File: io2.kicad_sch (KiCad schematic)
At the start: 67 parts, among them IC1 ILD217T, IC2 ILD217T, Q10 BC846, Q11 BC846, Q8 BC846, Q9 BC846, U11 74HC14, U12 74HC165, X3 Conn_DI

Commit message: Ref 2.4
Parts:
- removed PS2: 1S4E_0505S1U, custom_th:Converter_DCDC_GAPTEC_1S4E_S1U, symbol Converter_DCDC:MEE1S0303SC
- added PS2: (no value), symbol lcsc:B0505S-1WR2_C909796
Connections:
- net +5V: now also C13.2, PS2.2 (Vin); no longer C13.1
- net 5V_1: now also PS2.4 (Vo)
- net GND: now also C13.1, PS2.1 (GND); no longer C13.2
- net GND1: now also PS2.3 (0V)
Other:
- moved on the sheet: C13
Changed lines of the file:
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@@
   (title_block
     (title "BSC")
-    (date "2023-03-30")
-    (rev "2.3")
+    (date "2023-06-25")
+    (rev "2.4")
   )
   (junction (at 115.57 118.745) (diameter 0) (color 0 0 0 0)
   )
-  (junction (at 171.45 154.305) (diameter 0) (color 0 0 0 0)
-  )
-  (junction (at 171.45 149.225) (diameter 0) (color 0 0 0 0)
-  )
   (junction (at 95.885 29.21) (diameter 0) (color 0 0 0 0)
   )
@@
   (junction (at 229.87 57.785) (diameter 0) (color 0 0 0 0)
   )
+  (junction (at 165.735 149.225) (diameter 0) (color 0 0 0 0)
+  )
   (junction (at 29.845 144.145) (diameter 0) (color 0 0 0 0)
   )
@@
   )
   (junction (at 115.57 132.715) (diameter 0) (color 0 0 0 0)
+  )
+  (junction (at 165.735 154.305) (diameter 0) (color 0 0 0 0)
   )
   (junction (at 38.735 154.305) (diameter 0) (color 0 0 0 0)
@@
     (stroke (width 0) (type default) (color 0 0 0 0))
   )
-  (wire (pts (xy 171.45 149.225) (xy 172.72 149.225))
-    (stroke (width 0) (type default) (color 0 0 0 0))
-  )
   (wire (pts (xy 55.88 31.75) (xy 67.945 31.75))
     (stroke (width 0) (type default) (color 0 0 0 0))
@@
     (stroke (width 0) (type default) (color 0 0 0 0))
   )
+  (wire (pts (xy 160.02 141.605) (xy 165.735 141.605))
+    (stroke (width 0) (type default) (color 0 0 0 0))
+  )
   (wire (pts (xy 38.735 54.61) (xy 55.88 54.61))
     (stroke (width 0) (type default) (color 0 0 0 0))
@@
     (stroke (width 0) (type default) (color 0 0 0 0))
   )
-  (wire (pts (xy 172.72 154.305) (xy 171.45 154.305))
-    (stroke (width 0) (type default) (color 0 0 0 0))
-  )
   (wire (pts (xy 255.905 24.765) (xy 260.985 24.765))
     (stroke (width 0) (type default) (color 0 0 0 0))
@@
     (stroke (width 0) (type default) (color 0 0 0 0))
   )
+  (wire (pts (xy 165.735 160.02) (xy 165.735 154.305))
+    (stroke (width 0) (type default) (color 0 0 0 0))
+  )
   (wire (pts (xy 38.735 117.475) (xy 38.735 115.57))
     (stroke (width 0) (type default) (color 0 0 0 0))
@@
     (stroke (width 0) (type default) (color 0 0 0 0))
   )
+  (wire (pts (xy 165.735 149.225) (xy 170.18 149.225))
+    (stroke (width 0) (type default) (color 0 0 0 0))
+  )
   (wire (pts (xy 26.67 166.37) (xy 26.67 182.88))
     (stroke (width 0) (type default) (color 0 0 0 0))
@@
     (stroke (width 0) (type default) (color 0 0 0 0))
   )
+  (wire (pts (xy 160.02 160.02) (xy 165.735 160.02))
+    (stroke (width 0) (type default) (color 0 0 0 0))
+  )
   (wire (pts (xy 66.675 126.365) (xy 66.675 160.655))
     (stroke (width 0) (type default) (color 0 0 0 0))
@@
     (stroke (width 0) (type default) (color 0 0 0 0))
   )
+  (wire (pts (xy 165.735 141.605) (xy 165.735 149.225))
+    (stroke (width 0) (type default) (color 0 0 0 0))
+  )
   (wire (pts (xy 67.945 123.825) (xy 65.405 123.825))
     (stroke (width 0) (type default) (color 0 0 0 0))
   )
-  (wire (pts (xy 171.45 146.685) (xy 171.45 149.225))
-    (stroke (width 0) (type default) (color 0 0 0 0))
-  )
   (wire (pts (xy 26.67 127.635) (xy 26.67 144.145))
     (stroke (width 0) (type default) (color 0 0 0 0))
@@
     (stroke (width 0) (type default) (color 0 0 0 0))
   )
-  (wire (pts (xy 171.45 154.305) (xy 171.45 155.575))
-    (stroke (width 0) (type default) (color 0 0 0 0))
-  )
   (wire (pts (xy 65.405 64.77) (xy 55.88 64.77))
     (stroke (width 0) (type default) (color 0 0 0 0))
@@
     (stroke (width 0) (type default) (color 0 0 0 0))
   )
+  (wire (pts (xy 165.735 154.305) (xy 170.18 154.305))
+    (stroke (width 0) (type default) (color 0 0 0 0))
+  )
   (wire (pts (xy 14.605 154.305) (xy 20.32 154.305))
     (stroke (width 0) (type default) (color 0 0 0 0))
@@
   )
   (wire (pts (xy 196.85 149.225) (xy 205.105 149.225))
+    (stroke (width 0) (type default) (color 0 0 0 0))
+  )
+  (wire (pts (xy 160.02 142.875) (xy 160.02 141.605))
     (stroke (width 0) (type default) (color 0 0 0 0))
   )
@@
     (pin "2")
   )
-  (symbol (lib_id "power:+5V") (at 171.45 146.685 0) (unit 1)
-    (in_bom yes) (on_board yes)
-    (property "Reference" "#PWR035" (id 0) (at 171.45 150.495 0)
-      (effects (font (size 1.27 1.27)) hide)
-    )
-    (property "Value" "+5V" (id 1) (at 171.45 143.1092 0))
-    (property "Footprint" "" (id 2) (at 171.45 146.685 0)
-      (effects (font (size 1.27 1.27)) hide)
-    )
-    (property "Datasheet" "" (id 3) (at 171.45 146.685 0)
+  (symbol (lib_id "power:+5V") (at 160.02 160.02 0) (unit 1)
+    (in_bom yes) (on_board yes)
+    (property "Reference" "#PWR035" (id 0) (at 160.02 163.83 0)
+      (effects (font (size 1.27 1.27)) hide)
+    )
+    (property "Value" "+5V" (id 1) (at 160.02 156.4442 0))
+    (property "Footprint" "" (id 2) (at 160.02 160.02 0)
+      (effects (font (size 1.27 1.27)) hide)
+    )
+    (property "Datasheet" "" (id 3) (at 160.02 160.02 0)
       (effects (font (size 1.27 1.27)) hide)
     )
@@
     (pin "2")
   )
+  (symbol (lib_id "lcsc:B0505S-1WR2_C909796") (at 182.88 151.765 0) (unit 1)
+    (in_bom yes) (on_board yes) (fields_autoplaced)
+    (property "Reference" "PS2" (id 0) (at 181.61 143.1122 0))
+    (property "Value" "" (id 1) (at 181.61 145.6491 0))
+    (property "Footprint" "" (id 2) (at 182.88 161.925 0)
+      (effects (font (size 1.27 1.27)) hide)
+    )
+    (property "Datasheet" "https://lcsc.com/product-detail/Power-Modules_DEXU-Electronics-B0505S-1WR2_C909796.html" (id 3) (at 182.88 164.465 0)
+      (effects (font (size 1.27 1.27)) hide)
+    )
+    (property "Manufacturer" "DEXU(德旭电子)" (id 4) (at 182.88 167.005 0)
+      (effects (font (size 1.27 1.27)) hide)
+    )
+    (property "LCSC Part" "C909796" (id 5) (at 182.88 169.545 0)
+      (effects (font (size 1.27 1.27)) hide)
+    )
+    (property "JLC Part" "Extended Part" (id 6) (at 182.88 172.085 0)
+      (effects (font (size 1.27 1.27)) hide)
+    )
+    (pin "1")
+    (pin "2")
+    (pin "3")
+    (pin "4")
+  )
   (symbol (lib_id "power:+3V3") (at 255.905 21.59 0) (unit 1)
     (in_bom yes) (on_board yes) (fields_autoplaced)
@@
     (pin "2")
   )
-  (symbol (lib_id "Converter_DCDC:MEE1S0303SC") (at 182.88 151.765 0) (unit 1)
-    (in_bom yes) (on_board yes) (fields_autoplaced)
-    (property "Reference" "PS2" (id 0) (at 182.88 142.9852 0))
-    (property "Value" "1S4E_0505S1U" (id 1) (at 182.88 145.5221 0))
-    (property "Footprint" "custom_th:Converter_DCDC_GAPTEC_1S4E_S1U" (id 2) (at 156.21 158.115 0)
-      (effects (font (size 1.27 1.27)) (justify left) hide)
-    )
-    (property "Datasheet" "https://power.murata.com/pub/data/power/ncl/kdc_mee1.pdf" (id 3) (at 209.55 159.385 0)
-      (effects (font (size 1.27 1.27)) (justify left) hide)
-    )
-    (pin "1")
-    (pin "2")
-    (pin "3")
-    (pin "4")
-  )
   (symbol (lib_id "power:GND") (at 115.57 44.45 0) (unit 1)
     (in_bom yes) (on_board yes)
@@
     (pin "1")
   )
-  (symbol (lib_id "Device:C_Small") (at 171.45 151.765 0) (unit 1)
-    (in_bom yes) (on_board yes)
-    (property "Reference" "C13" (id 0) (at 167.64 150.495 0)
-      (effects (font (size 1.27 1.27)) (justify left))
-    )
-    (property "Value" "100n" (id 1) (at 165.1 153.67 0)
-      (effects (font (size 1.27 1.27)) (justify left))
-    )
-    (property "Footprint" "Capacitor_SMD:C_0603_1608Metric" (id 2) (at 171.45 151.765 0)
-      (effects (font (size 1.27 1.27)) hide)
-    )
-    (property "Datasheet" "~" (id 3) (at 171.45 151.765 0)
+  (symbol (lib_id "Device:C_Small") (at 165.735 151.765 0) (unit 1)
+    (in_bom yes) (on_board yes)
+    (property "Reference" "C13" (id 0) (at 161.925 150.495 0)
+      (effects (font (size 1.27 1.27)) (justify left))
+    )
+    (property "Value" "100n" (id 1) (at 159.385 153.67 0)
+      (effects (font (size 1.27 1.27)) (justify left))
+    )
+    (property "Footprint" "Capacitor_SMD:C_0603_1608Metric" (id 2) (at 165.735 151.765 0)
+      (effects (font (size 1.27 1.27)) hide)
+    )
+    (property "Datasheet" "~" (id 3) (at 165.735 151.765 0)
       (effects (font (size 1.27 1.27)) hide)
     )
@@
     (pin "8")
   )
-  (symbol (lib_id "power:GND") (at 171.45 155.575 0) (unit 1)
-    (in_bom yes) (on_board yes)
-    (property "Reference" "#PWR036" (id 0) (at 171.45 161.925 0)
-      (effects (font (size 1.27 1.27)) hide)
-    )
-    (property "Value" "GND" (id 1) (at 171.45 160.0184 0))
-    (property "Footprint" "" (id 2) (at 171.45 155.575 0)
-      (effects (font (size 1.27 1.27)) hide)
-    )
-    (property "Datasheet" "" (id 3) (at 171.45 155.575 0)
-      (effects (font (size 1.27 1.27)) hide)
-    )
+  (symbol (lib_id "power:GND") (at 160.02 142.875 0) (unit 1)
+    (in_bom yes) (on_board yes)
+    (property "Reference" "#PWR036" (id 0) (at 160.02 149.225 0)
+      (effects (font (size 1.27 1.27)) hide)
+    )
+    (property "Value" "GND" (id 1) (at 160.02 147.3184 0))
+    (property "Footprint" "" (id 2) (at 160.02 142.875 0)
+      (effects (font (size 1.27 1.27)) hide)
+    )
+    (property "Datasheet" "" (id 3) (at 160.02 142.875 0)
+      (effects (font (size 1.27 1.27)) hide)
+    )

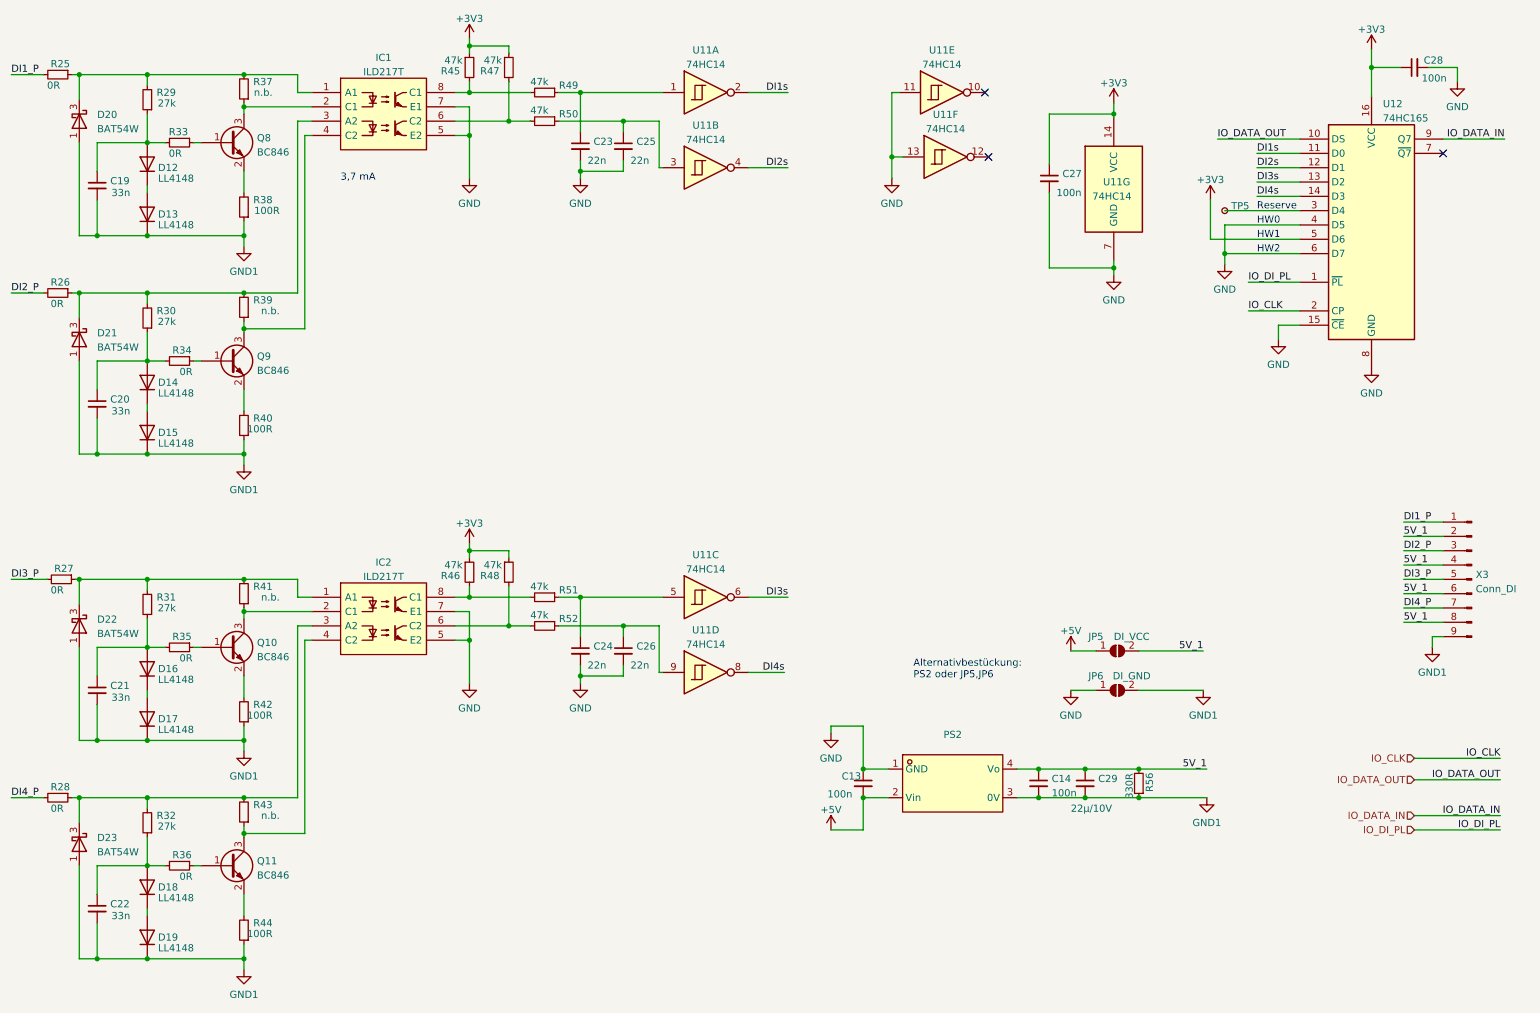
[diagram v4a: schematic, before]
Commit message: Improvements added (Ref 2.4.1)
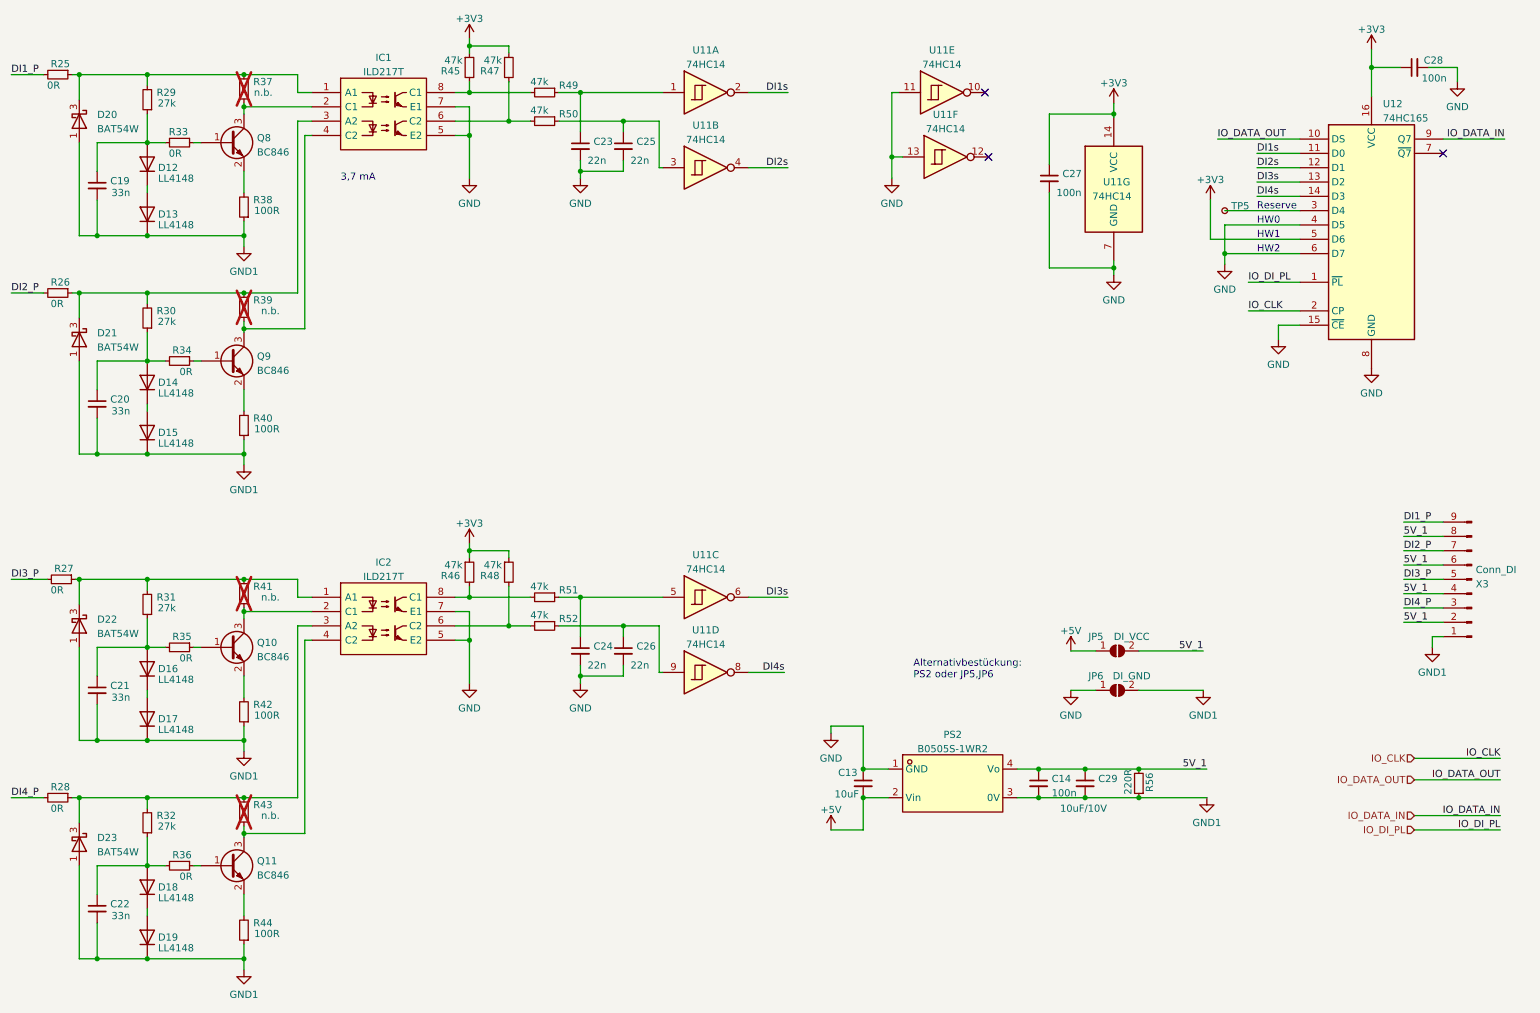
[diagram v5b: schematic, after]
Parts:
- C13: value 100n -> 10uF
- C29: value 22µ/10V -> 10uF/10V
- PS2: value (none) -> B0505S-1WR2; footprint (none) -> lcsc:PWRM-TH_BXXXXS-1WR3
- R37, R39, R41, R43: now not fitted
- R56: value 330R -> 220R; footprint Resistor_SMD:R_0603_1608Metric -> Resistor_SMD:R_0805_2012Metric
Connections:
- net DI1_P: now also X3.9 (Pin_9); no longer X3.1 (Pin_1)
- net DI2_P: now also X3.7 (Pin_7); no longer X3.3 (Pin_3)
- net DI4_P: now also X3.3 (Pin_3); no longer X3.7 (Pin_7)
- net GND1: now also X3.1 (Pin_1); no longer X3.9 (Pin_9)
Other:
- moved on the sheet: X3
